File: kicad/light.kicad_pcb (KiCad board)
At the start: 4 copper layers, 58 x 40 mm, 142 parts, among them J2 USB_C_Receptacle_USB2.0_16P, J3 Barrell Jack, J4 01x04, J5 SM03B-SRSS-TB, J6 SM03B-SRSS-TB, J9 Conn_01x09_MountingPin, Q1 NMOS, Q2 NMOS, Q3 NMOS, SW1 Boot, SW3 On/Off, SW4 Mode, U1 RP2350A-QFN60, U10 MAX6816, U2 TPS5405DR, U3 W25Q128JVS, U4 LBEE5KL1YN-814, U5 TPS2115ADRBR, U6 TPS2120, U7 HDC1080, U8 MAX6816, U9 MAX6816, Y1 ABM8-272-T3

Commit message: x review
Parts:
- moved R29 1.92 mm to (163.7, 85.6)
- moved C41 1.91 mm to (138.6, 114.7)
- moved R41 1.24 mm to (136.1, 110.6), turned to 180 degrees
- moved R28 0.61 mm to (163.7, 83.6)
- moved D73 0.50 mm to (166.3, 111.5)
- moved R44 0.50 mm to (166.3, 108.8)
- moved C40 0.48 mm to (151.0, 113.1), turned to 90 degrees
- moved Q1 0.46 mm to (166.2, 80.0)
- moved Q2 0.46 mm to (166.2, 83.5)
- moved Q3 0.46 mm to (166.2, 87.0)
- moved R27 0.46 mm to (163.7, 80.4)
- moved TP5 0.41 mm to (167.8, 82.1)
- moved TP6 0.41 mm to (167.8, 84.6)
- moved TP7 0.41 mm to (167.8, 87.1)
- moved J2 0.35 mm to (129.4, 95.6)
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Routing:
- net /WE_SDA: track 62.1 -> 46.3 mm, vias 4 -> 2
- net GND: track 33.6 -> 21.4 mm, vias 117 -> 121
- net /ROT_ENC_A: track 48.6 -> 44.1 mm
- net /WL_GPIO1: track 43.3 -> 40.9 mm
- net /QSPI_SD1: track 16.2 -> 18.5 mm
- net /ROT_ENC_B: track 54.1 -> 51.7 mm
- net /BTN_MODE: track 70.0 -> 68.2 mm, vias 4 -> 2
- net Net-(Q3-G): track 5.85 -> 7.48 mm
- net +1V1: track 27.4 -> 29.0 mm
- net /GPIO2: track 54.9 -> 56.3 mm, vias 0 -> 1
- net /BTN_ON_OFF: track 59.9 -> 58.9 mm
- net /WL_D: track 31.9 -> 30.9 mm
- net +12V: track 33.2 -> 32.4 mm
- net /WE_SCL: track 37.2 -> 37.8 mm
- net /USB_D-: track 27.1 -> 26.5 mm
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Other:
- board text added: "+12v"
- board text added: "rev 4 2025-08-09"
- board text removed: "rev 3 2025-08-07"

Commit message: routing improvements
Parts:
- C38: footprint Capacitor_SMD:C_0603_1608Metric -> Capacitor_SMD:C_0805_2012Metric
- moved C40 1.85 mm to (151.9, 114.7), turned to -90 degrees
- moved C38 1.29 mm to (154.9, 79.8), turned to -90 degrees
- moved R13 0.39 mm to (138.8, 109.5), turned to 180 degrees
- moved C5 0.10 mm to (137.2, 108.3)
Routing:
- net /BTN_ON_OFF: track 58.9 -> 33.0 mm
- net /BTN_MODE: track 68.2 -> 44.0 mm
- net +3V3: track 155.0 -> 145.9 mm, vias 9 -> 12
- net /WL_CS: track 21.5 -> 25.4 mm
- net /V_RGB: track 15.8 -> 19.4 mm
- net /PWR_DRGB_LVL: track 33.5 -> 30.0 mm
- net +12V: track 32.4 -> 29.7 mm
- net Net-(U10-IN): track 8.58 -> 11.2 mm
- net /ROT_ENC_A: track 44.1 -> 46.5 mm
- net GND: track 21.4 -> 23.1 mm, vias 121 -> 128
- net /WL_ON: track 30.1 -> 31.7 mm
- net /GPIO2: track 56.3 -> 54.8 mm
- net /VRGB_OUT: track 9.34 -> 8.07 mm
- net /ROT_ENC_SW: track 42.0 -> 42.6 mm
- net /GPIO1: track 71.4 -> 70.9 mm
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
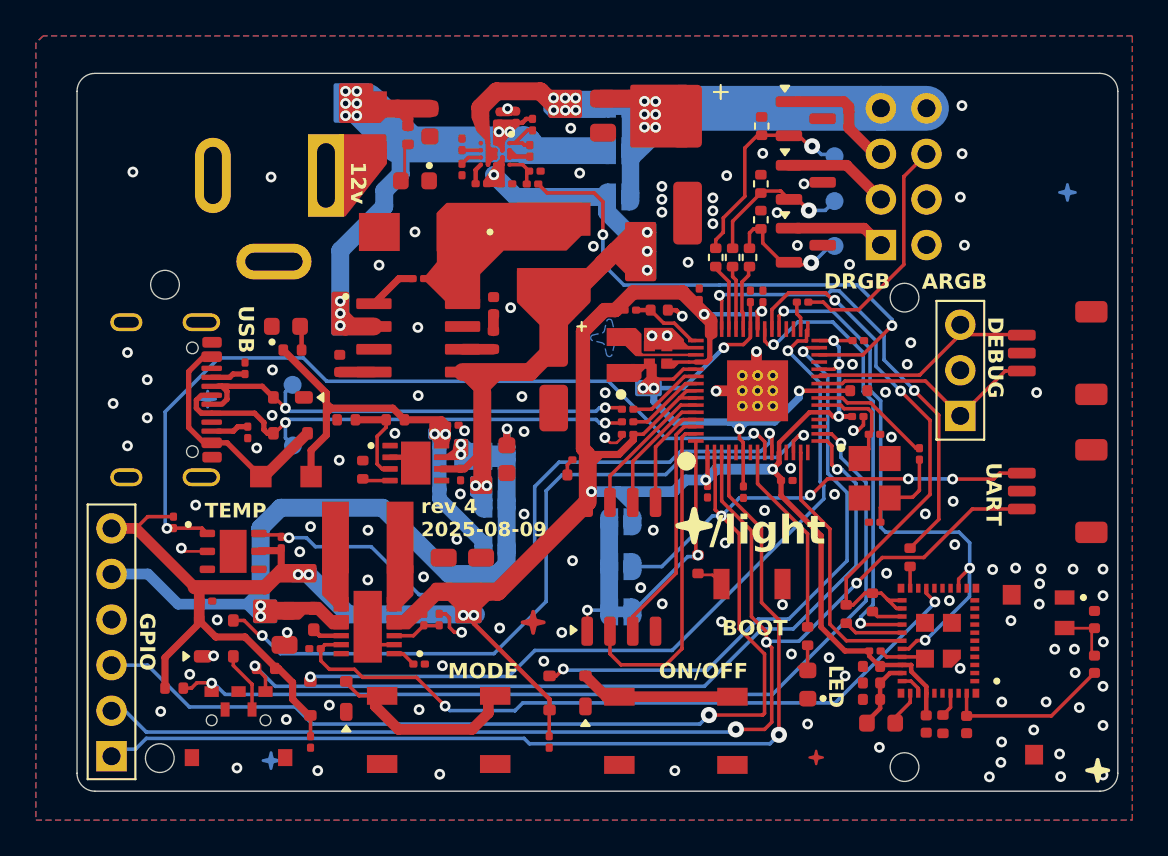
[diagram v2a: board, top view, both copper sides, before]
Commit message: improve layout; increase space between components
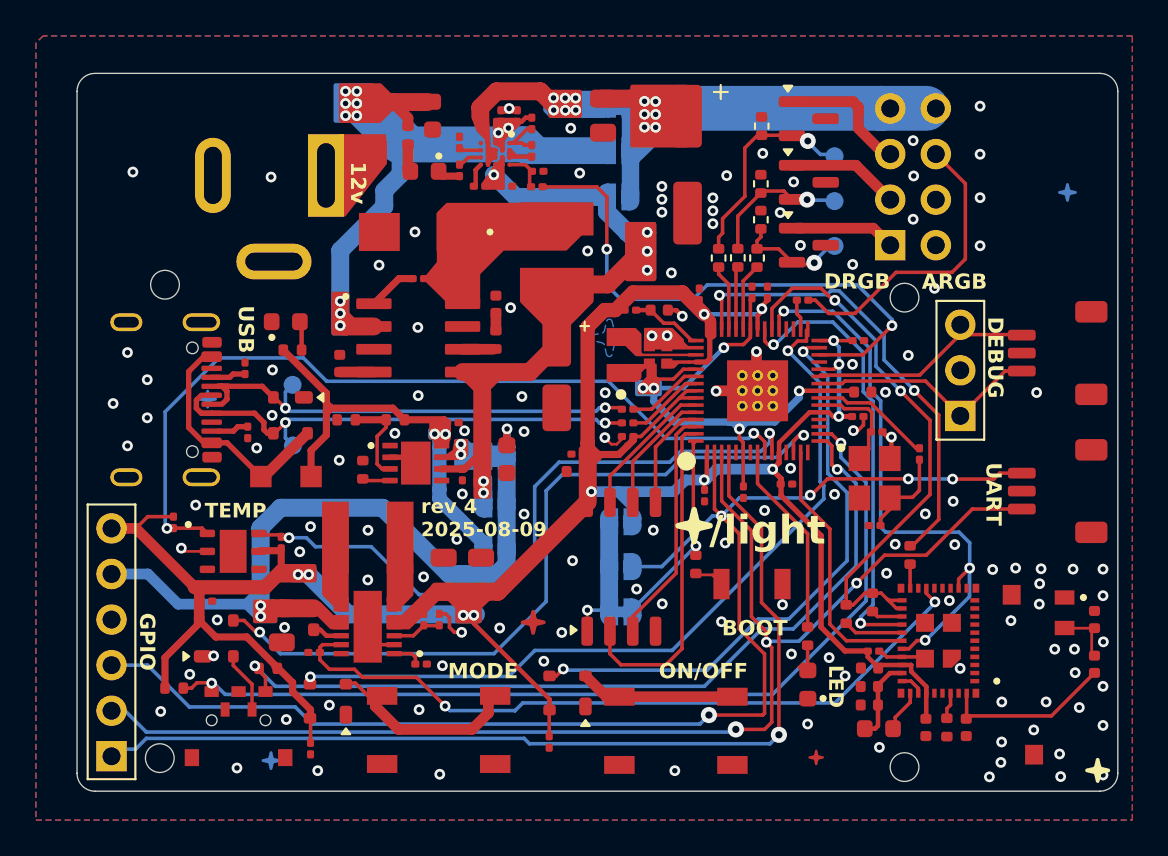
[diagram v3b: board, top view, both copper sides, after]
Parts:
- moved D68 0.75 mm to (144.9, 82.9)
- moved J4 0.52 mm to (170.9, 87.0)
- moved R32 0.42 mm to (163.5, 87.7)
- moved C24 0.41 mm to (145.4, 79.8)
- moved C41 0.37 mm to (138.6, 115.1)
- moved C13 0.33 mm to (164.1, 89.7)
- moved C30 0.33 mm to (169.7, 112.6)
- moved L4 0.33 mm to (170.3, 114.0)
- moved C18 0.32 mm to (153.5, 98.7)
- moved R31 0.29 mm to (162.4, 87.7)
- moved R22 0.28 mm to (174.1, 113.9)
- moved R38 0.28 mm to (151.2, 83.8)
- moved C12 0.27 mm to (160.6, 101.0)
- moved D67 0.26 mm to (137.2, 91.3)
- moved C8 0.24 mm to (163.2, 89.7)
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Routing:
- net /ARGB-DATA: track 13.2 -> 16.7 mm
- net /VREG5: track 38.5 -> 35.8 mm
- net GND: track 23.1 -> 25.4 mm, vias 128 -> 132
- net +3V3: track 145.9 -> 148.1 mm
- net /VSYS: track 33.6 -> 35.4 mm
- net /PWR_DRGB_LVL: track 30.0 -> 31.2 mm
- net Net-(D68-A): track 2.43 -> 1.55 mm
- net Net-(Q3-G): track 7.48 -> 6.63 mm
- net /VIN_LDO: track 4.00 -> 4.69 mm
- net Net-(Q1-G): track 12.0 -> 11.5 mm
- net Net-(Q2-G): track 8.55 -> 8.01 mm
- net Net-(J4-Pin_7): track 5.05 -> 5.57 mm

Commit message: general layour improvements
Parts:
- C35: value 1000u -> 470u
- Q1, Q2, Q3: value NMOS -> IRLML6344
- moved TP6 0.95 mm to (167.8, 85.5)
- moved TP7 0.95 mm to (167.8, 88.0)
- moved TP5 0.37 mm to (167.8, 82.4)
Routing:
- net +3V3: track 148.1 -> 149.9 mm
- net Net-(Q1-G): track 11.5 -> 12.4 mm
- net Net-(Q3-G): track 6.63 -> 5.87 mm
- net Net-(Q2-G): track 8.01 -> 8.57 mm
- net GND: vias 132 -> 138

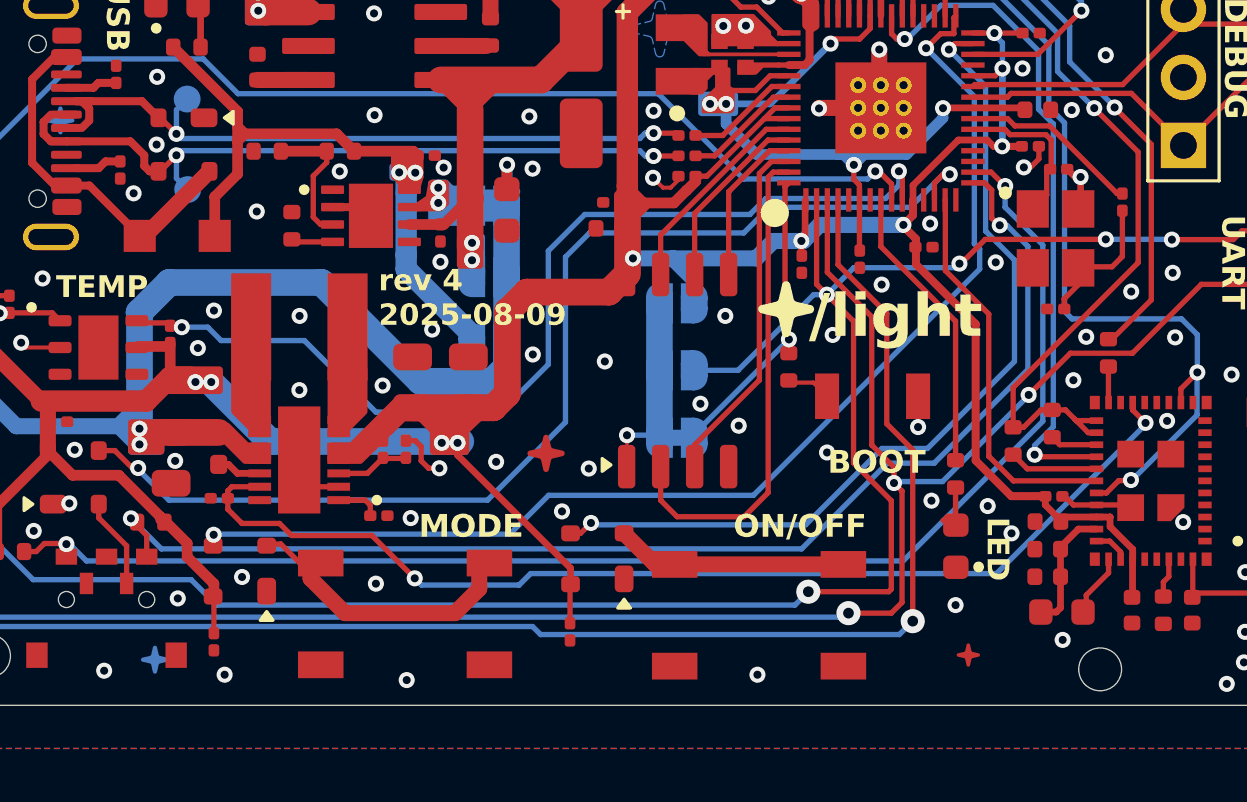
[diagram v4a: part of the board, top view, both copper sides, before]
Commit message: rev 5; replaced single RED LED with added 2x2 RGB LEDs
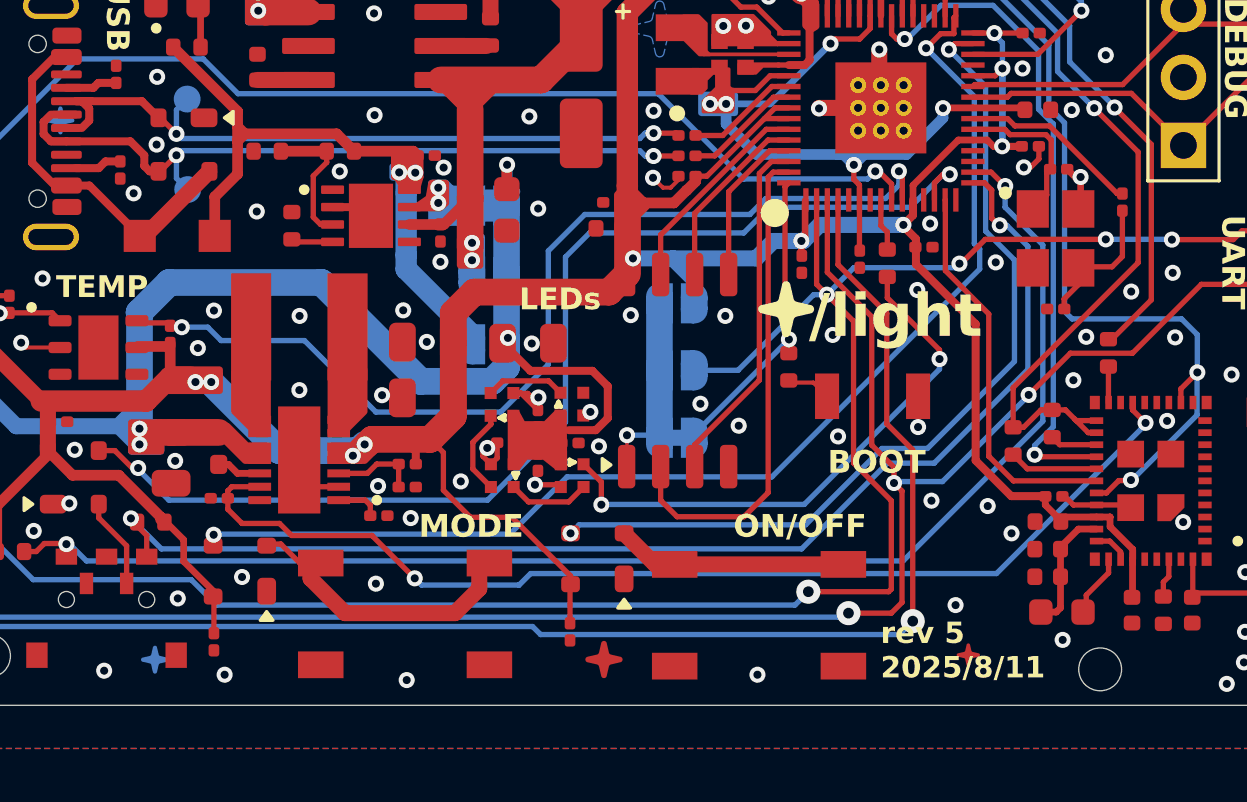
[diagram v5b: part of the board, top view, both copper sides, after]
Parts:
- removed D73: LED Green, LED_SMD:LED_0603_1608Metric
- added C48: 100u, Capacitor_SMD:C_0805_2012Metric, F.Cu at (150.3, 103.9)
- added C49: 0.1u, Capacitor_SMD:C_0201_0603Metric, F.Cu at (150.7, 108.4)
- added C50: 0.1u, Capacitor_SMD:C_0201_0603Metric, F.Cu at (151.9, 107.6)
- added C52: 0.1u, Capacitor_SMD:C_0201_0603Metric, F.Cu at (150.7, 106.7)
- added C53: 0.1u, Capacitor_SMD:C_0201_0603Metric, F.Cu at (149.5, 107.6)
- added D1: WS2812B-1010, WS2812B_1010:WS2812B_1010, F.Cu at (152.0, 108.9)
- added D3: WS2812B-1010, WS2812B_1010:WS2812B_1010, F.Cu at (149.4, 106.2)
- added D4: WS2812B-1010, WS2812B_1010:WS2812B_1010, F.Cu at (149.4, 108.9)
- added D5: WS2812B-1010, WS2812B_1010:WS2812B_1010, F.Cu at (152.0, 106.2)
- R44: value 120 -> 330
- moved R44 8.27 mm to (163.8, 100.9)
- moved C21 2.13 mm to (146.6, 103.9), turned to 180 degrees
- moved R15 1.41 mm to (145.8, 109.3), turned to 0 degrees
- moved R14 1.06 mm to (145.8, 108.4), turned to 180 degrees
- moved C22 0.81 mm to (146.6, 106.0), turned to 180 degrees
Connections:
- R44 pad 2: Net-(D73-A) -> /BOARD_RGB_DATA
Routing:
- net /BOARD_RGB_DATA: track 0.00 -> 20.8 mm, vias 0 -> 2
- net /GPIO5: track 10.9 -> 1.95 mm
- net /VSYS: track 35.4 -> 42.8 mm, vias 3 -> 4
- net GND: track 25.4 -> 28.6 mm, vias 138 -> 142
- net Net-(D3-DIN): track 0.00 -> 3.09 mm
- net Net-(D1-DOUT): track 0.00 -> 3.07 mm
- net Net-(D3-DOUT): track 0.00 -> 2.98 mm
- net +3V3: track 149.9 -> 151.7 mm
- net Net-(D73-A): track 1.41 -> 0.00 mm
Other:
- board text added: "LEDs"
- board text added: "rev 5 2025/8/11"
- board text removed: "LED"
- board text removed: "rev 4 2025-08-09"

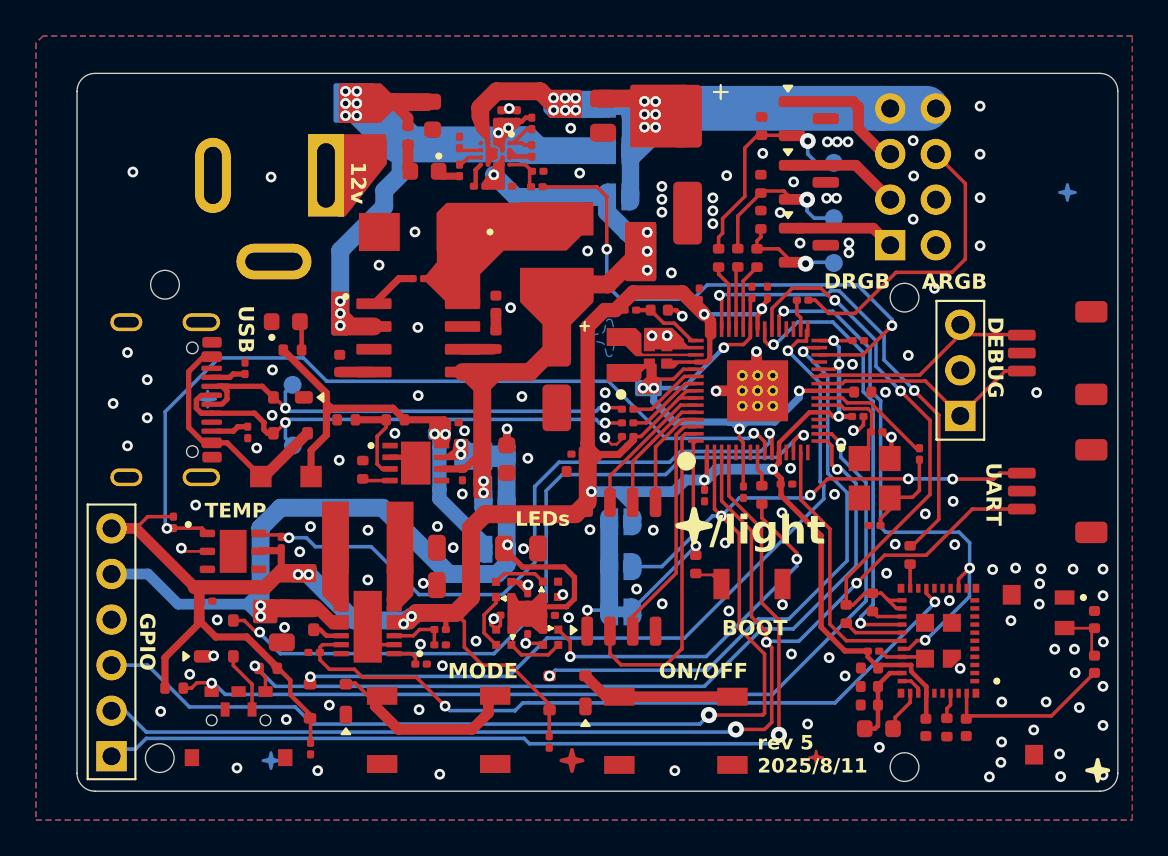
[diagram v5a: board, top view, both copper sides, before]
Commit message: shrink C27; layout improvements; prod is getting closer
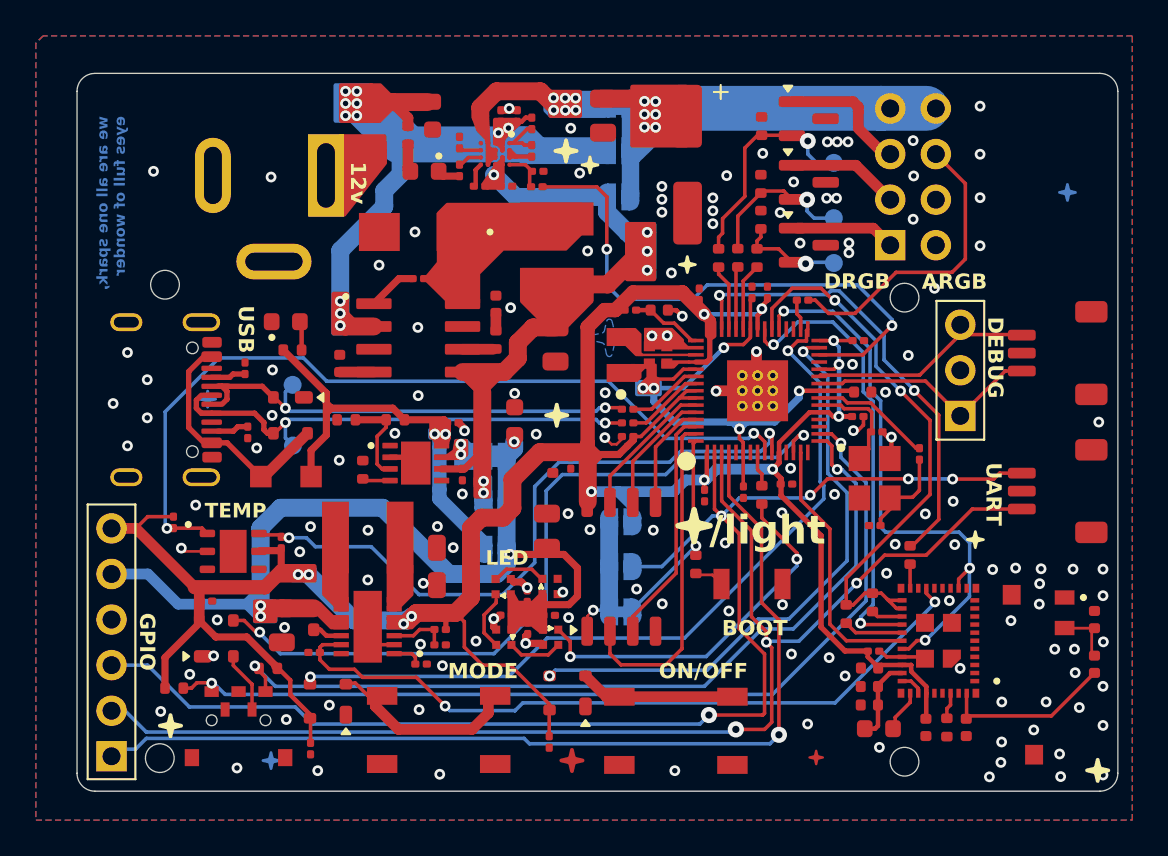
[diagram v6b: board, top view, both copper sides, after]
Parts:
- C27: footprint Capacitor_SMD:CP_Elec_4x5.4 -> Capacitor_SMD:C_0805_2012Metric
- moved C34 2.16 mm to (150.0, 96.8), turned to 90 degrees
- moved C48 1.75 mm to (151.8, 102.9), turned to 90 degrees
- moved C27 1.73 mm to (152.2, 92.5)
- moved C43 1.31 mm to (152.1, 99.2), turned to -90 degrees
- moved C18 0.61 mm to (153.1, 99.2), turned to -90 degrees
- moved TP9 0.44 mm to (167.8, 79.4)
- moved H4 0.30 mm to (171.7, 115.8)
- moved D3 0.16 mm to (149.3, 106.0)
- moved D5 0.16 mm to (151.9, 106.0)
- moved C52 0.16 mm to (150.7, 106.6)
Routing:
- net +3V3: track 151.7 -> 153.8 mm
- net /VREG5: track 35.8 -> 36.5 mm
- net GND: track 28.6 -> 28.0 mm
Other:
- board text added: "LED"
- board text removed: "LEDs"
- board text removed: "rev 5 2025/8/11"

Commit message: impedance matching ()yay)
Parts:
- moved R43 1.97 mm to (138.3, 91.0), turned to -90 degrees
- moved D75 0.91 mm to (137.2, 95.6)
- moved TP2 0.91 mm to (137.4, 97.3)
- moved TP3 0.91 mm to (137.3, 93.9)
- moved D67 0.50 mm to (136.7, 91.3), turned to 90 degrees
- moved R2 0.25 mm to (134.9, 97.7)
- moved R3 0.07 mm to (134.9, 93.9)
- moved SW3 0.06 mm to (158.9, 114.0)
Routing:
- net /USB_D+: track 27.8 -> 26.7 mm
- net /WE_SDA: track 46.3 -> 47.4 mm
- net /USB_D-: track 26.5 -> 25.4 mm
- net /VBUS: track 22.8 -> 23.7 mm
- net Net-(D70-A): track 13.1 -> 13.8 mm
- net GND: vias 142 -> 144
